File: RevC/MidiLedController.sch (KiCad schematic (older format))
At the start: 53 parts, among them J1 Molex 2Way KK254, J12 Barrel_Jack, SW1 SW_DIP_x04, SW2 SW_SPST, U20 STM32F051K8Tx, U21 6N135S

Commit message: updates
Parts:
- C26, C5: LcscNo (none) -> C152892; MouserNo 710-885012207027 -> (none); Type (none) -> N/A
- C28, C6: LcscNo (none) -> C94108; MouserNo 710-885012207098 -> (none); Type (none) -> N/A
- C32: LcscNo (none) -> C87998; MouserNo 791-0805X475M250CT -> (none); Type (none) -> N/A
- C33: LcscNo (none) -> C107135; MouserNo 710-885012207066 -> (none); Type (none) -> N/A
- C34: LcscNo (none) -> C376927; MouserNo 791-0805X105K100CT -> (none); Type (none) -> N/A
- D2, R4, R9: Type (none) -> N/A
- D_STATUS1, D_STATUS_2, D_STATUS_3, D_STATUS_4, D_STATUS_5, D_STATUS_6, D_STATUS_7, D_STATUS_8, D_STATUS_9, J1, J_AUX1, J_OUT1, J_OUT2, J_OUT3, J_OUT4, J_OUT5, J_OUT6, J_OUT7, J_OUT8, J_OUT9, SW1, SW2: EbayPurchase (none) -> True
- J12: EbayPurchase (none) -> True; MouserNo 502-RAPC722X -> (none)
- J_MIDI_IN1: EbayPurchase (none) -> True; RSComponentsNo 491-087 -> (none)
- R1: LcscNo (none) -> C115295; MouserNo 71-CRCW080510K0FKEAC -> (none); Type (none) -> N/A
- R119, R120, R121, R122: LcscNo (none) -> C25623; Type (none) -> N/A
- R25, R74: LcscNo (none) -> C106949; MouserNo 71-CRCW0805100RFKEAC -> (none); Type (none) -> N/A
- RV1: MouserNo (none) -> 652-PTH901-030S-103B; Type (none) -> PTH901-030S-103B1
- RV1: MouserNo (none) -> 652-PTH901-030S-103B; Type (none) -> PTH901-030S-103B

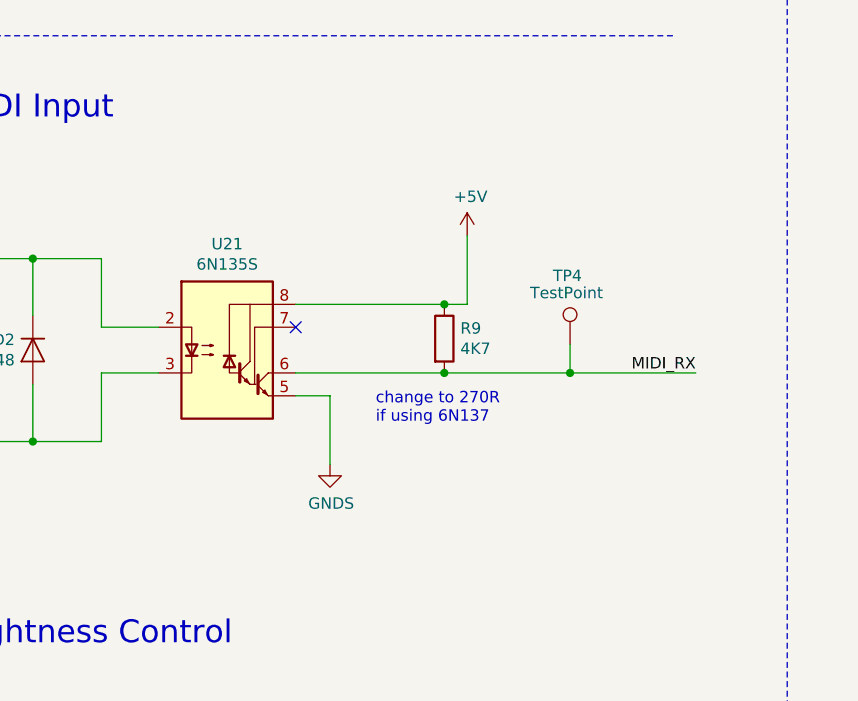
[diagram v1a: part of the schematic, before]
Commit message: Replaced 6N135 SMDIP8 with H11L1 SMDIP6
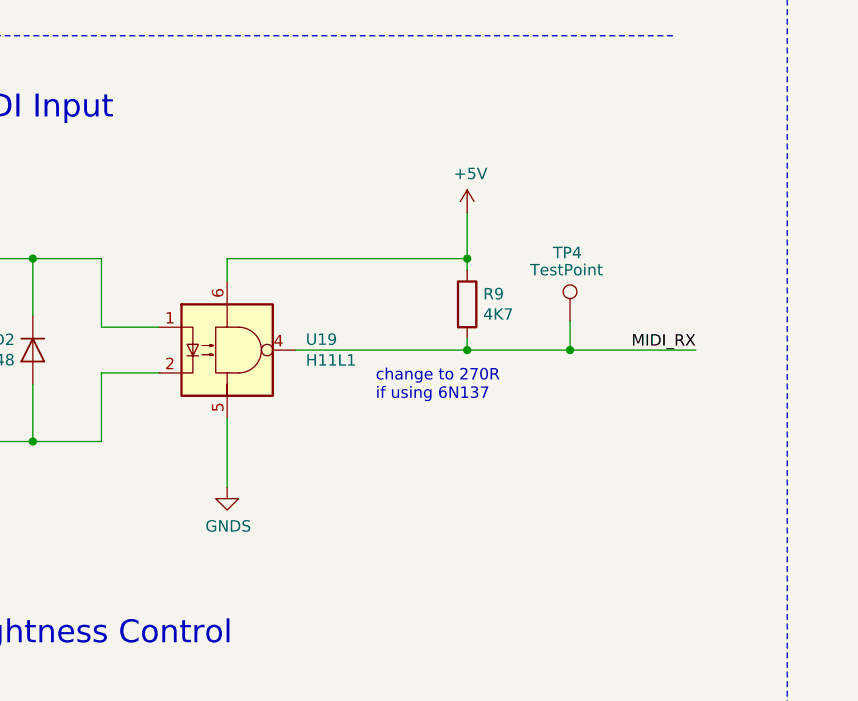
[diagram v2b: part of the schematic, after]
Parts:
- removed U21: 6N135S, Package_DIP:DIP-8_W8.89mm_SMDSocket_LongPads, symbol Isolator:6N139
- added U19: H11L1, Package_DIP:SMDIP-6_W9.53mm, symbol Isolator:H11L1
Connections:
- net +5V: now also U19.6
- net GNDS: now also U19.5
- net MIDI_RX: now also U19.4
- net at D2.1 (K), R4.1: now also U19.1
- net at D2.2 (A), J_MIDI_IN1.5: now also U19.2
- no-connect marks 9 -> 8
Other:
- moved on the sheet: R9, TP4
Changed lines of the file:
@@
 Text Notes 2475 16975 2    50   ~ 0
 USART TX (NOT USED)
-$Comp
-L Isolator:6N139 U21
-U 1 1 5DA8DB27
-P 3050 6525
-F 0 "U21" H 3050 6989 50  0000 C CNN
-F 1 "6N135S" H 3050 6900 50  0000 C CNN
-F 2 "Package_DIP:DIP-8_W8.89mm_SMDSocket_LongPads" H 3340 6225 50  0001 C CNN
-F 3 "https://optoelectronics.liteon.com/upload/download/DS70-2008-0032/6N135-L%206N136-L%20series.pdf" H 3340 6225 50  0001 C CNN
-F 4 "859-6N135S" H 3050 6525 50  0001 C CNN "MouserNo"
-	1    3050 6525
-	1    0    0    -1
-$EndComp
 Wire Wire Line
 	2500 6125 2500 6425
@@
 Wire Wire Line
 	2200 6925 2500 6925
-Wire Wire Line
-	3350 6625 4000 6625
-Text Label 5100 6625 2    50   ~ 0
+Text Label 5100 6525 2    50   ~ 0
 MIDI_RX
-Wire Wire Line
-	3350 6325 4000 6325
 $Comp
 L power:+5V #PWR016
 U 1 1 5DAD2B00
-P 4100 6025
-F 0 "#PWR016" H 4100 5875 50  0001 C CNN
-F 1 "+5V" H 4115 6196 50  0000 C CNN
-F 2 "" H 4100 6025 50  0001 C CNN
-F 3 "" H 4100 6025 50  0001 C CNN
-	1    4100 6025
-	1    0    0    -1
-$EndComp
-Wire Wire Line
-	4100 6025 4100 6325
+P 4100 5925
+F 0 "#PWR016" H 4100 5775 50  0001 C CNN
+F 1 "+5V" H 4115 6096 50  0000 C CNN
+F 2 "" H 4100 5925 50  0001 C CNN
+F 3 "" H 4100 5925 50  0001 C CNN
+	1    4100 5925
+	1    0    0    -1
+$EndComp
+Wire Wire Line
+	4100 5925 4100 6125
 $Comp
 L Device:R R9
 U 1 1 5DAD60A8
-P 4000 6475
-F 0 "R9" H 4070 6520 50  0000 L CNN
-F 1 "4K7" H 4070 6431 50  0000 L CNN
-F 2 "Resistor_SMD:R_0805_2012Metric_Pad1.15x1.40mm_HandSolder" V 3930 6475 50  0001 C CNN
-F 3 "~" H 4000 6475 50  0001 C CNN
-F 4 "279-CRGP0805F270R" H 4000 6475 50  0001 C CNN "MouserNo"
-F 5 "N/A" H 4000 6475 50  0001 C CNN "Type"
-	1    4000 6475
-	1    0    0    -1
-$EndComp
-Connection ~ 4000 6325
-Wire Wire Line
-	4000 6325 4100 6325
-Connection ~ 4000 6625
-Wire Wire Line
-	3350 6725 3500 6725
-Wire Wire Line
-	3500 6725 3500 7025
+P 4100 6325
+F 0 "R9" H 4170 6370 50  0000 L CNN
+F 1 "4K7" H 4170 6281 50  0000 L CNN
+F 2 "Resistor_SMD:R_0805_2012Metric_Pad1.15x1.40mm_HandSolder" V 4030 6325 50  0001 C CNN
+F 3 "~" H 4100 6325 50  0001 C CNN
+F 4 "279-CRGP0805F270R" H 4100 6325 50  0001 C CNN "MouserNo"
+F 5 "N/A" H 4100 6325 50  0001 C CNN "Type"
+	1    4100 6325
+	1    0    0    -1
+$EndComp
+Wire Wire Line
+	3050 6825 3050 7125
 $Comp
 L power:GNDS #PWR017
 U 1 1 5DAD903D
-P 3500 7025
-F 0 "#PWR017" H 3500 6775 50  0001 C CNN
-F 1 "GNDS" H 3505 6854 50  0000 C CNN
-F 2 "" H 3500 7025 50  0001 C CNN
-F 3 "" H 3500 7025 50  0001 C CNN
-	1    3500 7025
+P 3050 7125
+F 0 "#PWR017" H 3050 6875 50  0001 C CNN
+F 1 "GNDS" H 3055 6954 50  0000 C CNN
+F 2 "" H 3050 7125 50  0001 C CNN
+F 3 "" H 3050 7125 50  0001 C CNN
+	1    3050 7125
 	1    0    0    -1
 $EndComp
@@
 NoConn ~ 2525 16275
 NoConn ~ 3625 16775
-NoConn ~ 3350 6425
 Wire Wire Line
 	3225 15375 3225 15325
@@
 L Connector:TestPoint TP?
 U 1 1 5DDC4ABE
-P 4550 6500
+P 4550 6400
 AR Path="/5DE5D23A/5DDC4ABE" Ref="TP?"  Part="1"
 AR Path="/5DDC4ABE" Ref="TP4"  Part="1"
-F 0 "TP4" H 4475 6800 50  0000 L CNN
-F 1 "TestPoint" H 4375 6725 50  0000 L CNN
-F 2 "TestPoint:TestPoint_Pad_1.0x1.0mm" H 4750 6500 50  0001 C CNN
-F 3 "~" H 4750 6500 50  0001 C CNN
-	1    4550 6500
-	1    0    0    -1
-$EndComp
-Wire Wire Line
-	4550 6500 4550 6625
+F 0 "TP4" H 4475 6700 50  0000 L CNN
+F 1 "TestPoint" H 4375 6625 50  0000 L CNN
+F 2 "TestPoint:TestPoint_Pad_1.0x1.0mm" H 4750 6400 50  0001 C CNN
+F 3 "~" H 4750 6400 50  0001 C CNN
+	1    4550 6400
+	1    0    0    -1
+$EndComp
+Wire Wire Line
+	4550 6400 4550 6525
 $Comp
 L Connector:TestPoint TP?
@@
 	0    1    1    0
 $EndComp
-Text Notes 3700 6850 0    50   ~ 0
+Text Notes 3700 6750 0    50   ~ 0
 change to 270R  \nif using 6N137
-Connection ~ 4550 6625
-Wire Wire Line
-	4550 6625 5100 6625
-Wire Wire Line
-	4000 6625 4550 6625
+Connection ~ 4550 6525
+Wire Wire Line
+	4550 6525 5100 6525
 Wire Wire Line
 	13925 2200 14575 2200
@@
 	0    -1   1    0
 $EndComp
+$Comp
+L Isolator:H11L1 U19
+U 1 1 5E85A506
+P 3050 6525
+F 0 "U19" H 3394 6571 50  0000 L CNN
+F 1 "H11L1" H 3394 6480 50  0000 L CNN
+F 2 "Package_DIP:SMDIP-6_W9.53mm" H 2960 6525 50  0001 C CNN
+F 3 "https://www.fairchildsemi.com/datasheets/H1/H11L1M.pdf" H 2960 6525 50  0001 C CNN
+	1    3050 6525
+	1    0    0    -1
+$EndComp
+Wire Wire Line
+	3350 6525 4100 6525
+Wire Wire Line
+	3050 6125 4100 6125
+Wire Wire Line
+	4100 6175 4100 6125
+Connection ~ 4100 6125
+Wire Wire Line
+	4100 6475 4100 6525
+Connection ~ 4100 6525
+Wire Wire Line
+	4100 6525 4550 6525
+Wire Wire Line
+	3050 6125 3050 6225
 $EndSCHEMATC

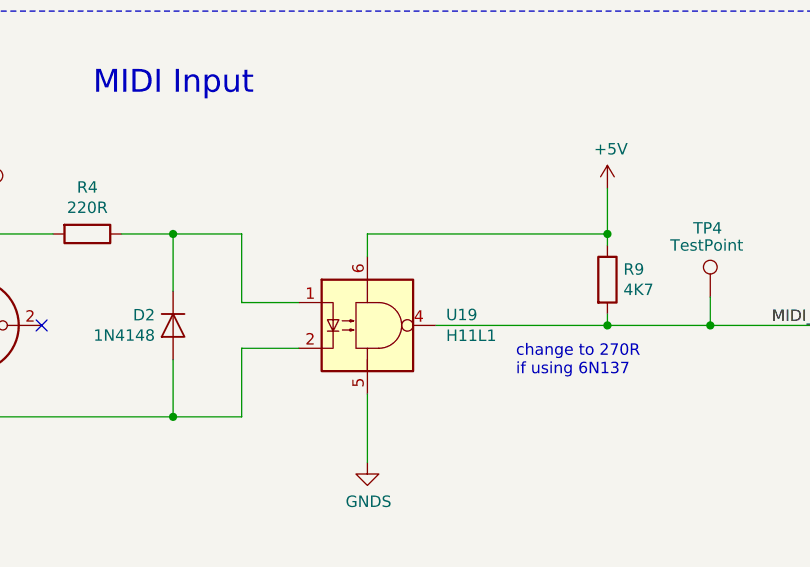
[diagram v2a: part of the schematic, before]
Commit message: Replaced H11L1 SMD6 with TLP2361 SO5
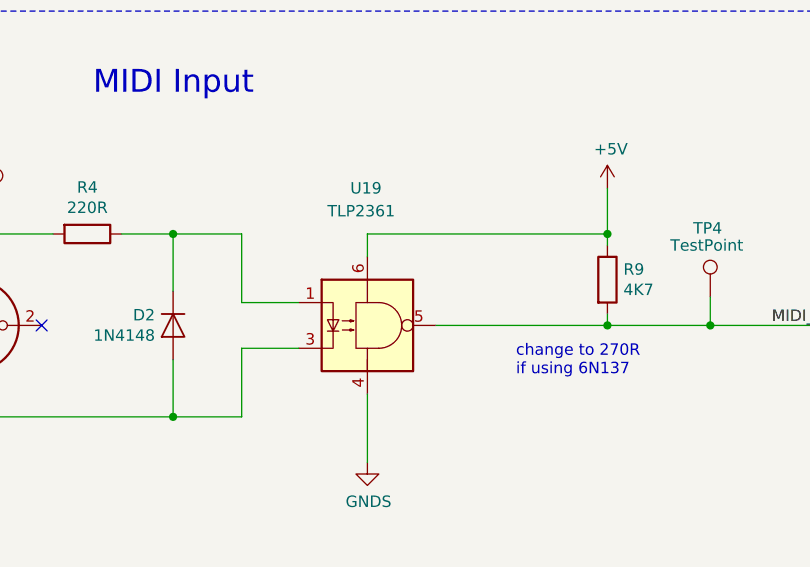
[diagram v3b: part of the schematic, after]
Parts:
- removed U19: H11L1, Package_DIP:SMDIP-6_W9.53mm, symbol Isolator:H11L1
- added U19: TLP2361, Package_SO:SO-6_4.4x3.6mm_P1.27mm, symbol TLP2361:TLP2361
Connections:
- net +5V: now also U19.6
- net GNDS: now also U19.4
- net MIDI_RX: now also U19.5
- net at D2.1 (K), R4.1: now also U19.1
- net at D2.2 (A), J_MIDI_IN1.5: now also U19.3
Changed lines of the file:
@@
 	0    -1   1    0
-$EndComp
-$Comp
-L Isolator:H11L1 U19
-U 1 1 5E85A506
-P 3050 6525
-F 0 "U19" H 3394 6571 50  0000 L CNN
-F 1 "H11L1" H 3394 6480 50  0000 L CNN
-F 2 "Package_DIP:SMDIP-6_W9.53mm" H 2960 6525 50  0001 C CNN
-F 3 "https://www.fairchildsemi.com/datasheets/H1/H11L1M.pdf" H 2960 6525 50  0001 C CNN
-	1    3050 6525
-	1    0    0    -1
 $EndComp
 Wire Wire Line
@@
 Wire Wire Line
 	3050 6125 3050 6225
+$Comp
+L TLP2361:TLP2361 U19
+U 1 1 5E7E54C8
+P 3050 6525
+F 0 "U19" H 2975 7125 50  0000 L CNN
+F 1 "TLP2361" H 2875 7025 50  0000 L CNN
+F 2 "Package_SO:SO-6_4.4x3.6mm_P1.27mm" H 2960 6525 50  0001 C CNN
+F 3 "https://datasheet.lcsc.com/szlcsc/TOSHIBA-TLP2361-V4-TPL-E_C123773.pdf" H 2960 6525 50  0001 C CNN
+	1    3050 6525
+	1    0    0    -1
+$EndComp
 $EndSCHEMATC
